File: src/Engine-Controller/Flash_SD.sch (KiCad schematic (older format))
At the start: 7 parts, among them P6 Micro_SD_Card, U5 SST25VF040B-50-4I-S2AE-T

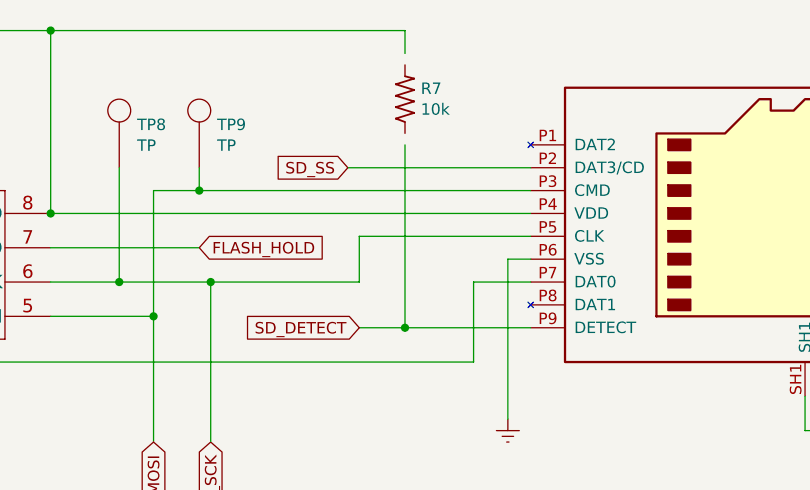
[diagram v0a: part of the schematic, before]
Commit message: Added Ignition System to lib and schematic
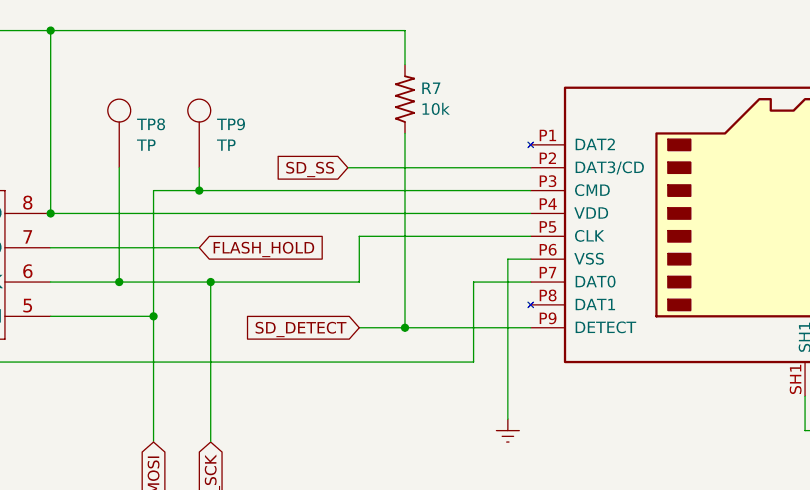
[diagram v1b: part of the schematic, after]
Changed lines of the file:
@@
 $Descr A4 11693 8268
 encoding utf-8
-Sheet 5 5
+Sheet 5 6
 Title "Data Logging Memory"
 Date "2021-07-03"
@@
 	0    -1   -1   0
 $EndComp
-Wire Wire Line
-	6600 3500 6600 4300
 Connection ~ 6600 4300
 Wire Wire Line
@@
 	4750 3000 5050 3000
 Wire Wire Line
-	6600 3000 6600 3100
-Wire Wire Line
 	5050 3000 5050 3800
 Connection ~ 5050 3000
 Wire Wire Line
 	5050 3000 6600 3000
+Wire Wire Line
+	6600 3450 6600 4300
+Wire Wire Line
+	6600 3000 6600 3150
 $EndSCHEMATC
